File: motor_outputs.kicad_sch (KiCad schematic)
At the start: 9 parts, among them J2 Conn_01x08

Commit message: BOM work
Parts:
- F1: LCSC (none) -> C70114
- F2: renamed from F4; LCSC (none) -> C70114
- F3: renamed from F2; LCSC (none) -> C70114
- F4: renamed from F3; LCSC (none) -> C70114
- J3: renamed from J2; LCSC (none) -> C5137858
- renumbered D7 to D5, D5 to D6, D6 to D7
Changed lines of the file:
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@@
-	(wire
-		(pts
-			(xy 77.47 78.74) (xy 93.98 78.74)
-		)
-		(stroke
-			(width 0)
-			(type default)
-		)
-	)
-	(wire
-		(pts
-			(xy 77.47 73.66) (xy 77.47 78.74)
-		)
-		(stroke
-			(width 0)
-			(type default)
-		)
-	)
 	(wire
 		(pts
@@
 	(wire
 		(pts
-			(xy 74.93 73.66) (xy 77.47 73.66)
-		)
-		(stroke
-			(width 0)
-			(type default)
-		)
-	)
-	(wire
-		(pts
-			(xy 99.06 50.8) (xy 99.06 85.09)
+			(xy 74.93 73.66) (xy 92.71 73.66)
+		)
+		(stroke
+			(width 0)
+			(type default)
+		)
+	)
+	(wire
+		(pts
+			(xy 99.06 46.99) (xy 99.06 85.09)
 		)
 		(stroke
@@
 	(wire
 		(pts
-			(xy 93.98 90.17) (xy 99.06 90.17)
+			(xy 92.71 90.17) (xy 99.06 90.17)
 		)
 		(stroke
@@
 	(wire
 		(pts
-			(xy 93.98 78.74) (xy 93.98 90.17)
+			(xy 92.71 73.66) (xy 92.71 90.17)
 		)
 		(stroke
@@
 	(wire
 		(pts
-			(xy 74.93 46.99) (xy 71.12 46.99)
+			(xy 71.12 46.99) (xy 99.06 46.99)
 		)
 		(stroke
@@
 		(pts
 			(xy 99.06 130.81) (xy 99.06 102.87)
-		)
-		(stroke
-			(width 0)
-			(type default)
-		)
-	)
-	(wire
-		(pts
-			(xy 74.93 50.8) (xy 74.93 46.99)
-		)
-		(stroke
-			(width 0)
-			(type default)
-		)
-	)
-	(wire
-		(pts
-			(xy 74.93 50.8) (xy 99.06 50.8)
 		)
 		(stroke
@@
 		(exclude_from_sim no)
 		(in_bom yes)
-		(on_board yes)
+		(on_board no)
 		(dnp no)
 		(fields_autoplaced yes)
-		(property "Reference" "F3"
+		(property "Reference" "F4"
 			(at 69.85 92.71 90)
 			(effects
@@
 		(property "Description" "Resettable fuse, polymeric positive temperature coefficient"
 			(at 69.85 99.06 0)
+			(effects
+				(font
+					(size 1.27 1.27)
+				)
+				(hide yes)
+			)
+		)
+		(property "LCSC" "C70114"
+			(at 69.85 99.06 90)
 			(effects
 				(font
@@
 			(project "barn-blinds-controller"
 				(path "/aa90962a-81b9-423d-8acd-c4e83fa798bb/4857807b-67c7-42cb-aab6-84b757102806"
-					(reference "F3")
+					(reference "F4")
 					(unit 1)
 				)
@@
 		(exclude_from_sim no)
 		(in_bom yes)
-		(on_board yes)
+		(on_board no)
 		(dnp no)
 		(fields_autoplaced yes)
-		(property "Reference" "F4"
+		(property "Reference" "F2"
 			(at 67.31 116.84 90)
 			(effects
@@
 		(property "Description" "Resettable fuse, polymeric positive temperature coefficient"
 			(at 67.31 123.19 0)
+			(effects
+				(font
+					(size 1.27 1.27)
+				)
+				(hide yes)
+			)
+		)
+		(property "LCSC" "C70114"
+			(at 67.31 123.19 90)
 			(effects
 				(font
@@
 			(project "barn-blinds-controller"
 				(path "/aa90962a-81b9-423d-8acd-c4e83fa798bb/4857807b-67c7-42cb-aab6-84b757102806"
-					(reference "F4")
+					(reference "F2")
 					(unit 1)
 				)
@@
 		(dnp no)
 		(fields_autoplaced yes)
-		(property "Reference" "D7"
+		(property "Reference" "D5"
 			(at 76.2 125.7299 0)
 			(effects
@@
 			(project "barn-blinds-controller"
 				(path "/aa90962a-81b9-423d-8acd-c4e83fa798bb/4857807b-67c7-42cb-aab6-84b757102806"
-					(reference "D7")
+					(reference "D5")
 					(unit 1)
 				)
@@
 		(exclude_from_sim no)
 		(in_bom yes)
-		(on_board yes)
+		(on_board no)
 		(dnp no)
 		(fields_autoplaced yes)
-		(property "Reference" "F2"
+		(property "Reference" "F3"
 			(at 69.85 67.31 90)
 			(effects
@@
 		(property "Description" "Resettable fuse, polymeric positive temperature coefficient"
 			(at 69.85 73.66 0)
+			(effects
+				(font
+					(size 1.27 1.27)
+				)
+				(hide yes)
+			)
+		)
+		(property "LCSC" "C70114"
+			(at 69.85 73.66 90)
 			(effects
 				(font
@@
 			(project "barn-blinds-controller"
 				(path "/aa90962a-81b9-423d-8acd-c4e83fa798bb/4857807b-67c7-42cb-aab6-84b757102806"
-					(reference "F2")
+					(reference "F3")
 					(unit 1)
 				)
@@
 		(dnp no)
 		(fields_autoplaced yes)
-		(property "Reference" "D5"
+		(property "Reference" "D6"
 			(at 78.74 76.1999 0)
 			(effects
@@
 			(project "barn-blinds-controller"
 				(path "/aa90962a-81b9-423d-8acd-c4e83fa798bb/4857807b-67c7-42cb-aab6-84b757102806"
-					(reference "D5")
+					(reference "D6")
 					(unit 1)
 				)
@@
 		(on_board yes)
 		(dnp no)
-		(property "Reference" "J2"
+		(property "Reference" "J3"
 			(at 106.68 95.2501 0)
 			(effects
@@
 		)
 		(property "Description" "Generic connector, single row, 01x08, script generated (kicad-library-utils/schlib/autogen/connector/)"
+			(at 104.14 95.25 0)
+			(effects
+				(font
+					(size 1.27 1.27)
+				)
+				(hide yes)
+			)
+		)
+		(property "LCSC" "C5137858"
 			(at 104.14 95.25 0)
 			(effects
@@
 			(project "barn-blinds-controller"
 				(path "/aa90962a-81b9-423d-8acd-c4e83fa798bb/4857807b-67c7-42cb-aab6-84b757102806"
-					(reference "J2")
+					(reference "J3")
 					(unit 1)
 				)
@@
 		(dnp no)
 		(fields_autoplaced yes)
-		(property "Reference" "D6"
+		(property "Reference" "D7"
 			(at 80.01 101.5999 0)
 			(effects
@@
 			(project "barn-blinds-controller"
 				(path "/aa90962a-81b9-423d-8acd-c4e83fa798bb/4857807b-67c7-42cb-aab6-84b757102806"
-					(reference "D6")
+					(reference "D7")
 					(unit 1)
 				)
@@
 		(exclude_from_sim no)
 		(in_bom yes)
-		(on_board yes)
+		(on_board no)
 		(dnp no)
 		(fields_autoplaced yes)
@@
 			(effects
 				(font
+					(size 1.27 1.27)
+				)
+				(hide yes)
+			)
+		)
+		(property "LCSC" "C70114"
+			(at 66.04 54.61 90)
+			(effects
+				(font

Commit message: Updated BOM, fixed a few components
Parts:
- F1, F2, F3, F4: LCSC C70114 -> C69691
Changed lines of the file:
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@@
 		(exclude_from_sim no)
 		(in_bom yes)
-		(on_board no)
+		(on_board yes)
 		(dnp no)
 		(fields_autoplaced yes)
@@
 			)
 		)
-		(property "LCSC" "C70114"
+		(property "LCSC" "C69691"
 			(at 69.85 99.06 90)
 			(effects
@@
 		(exclude_from_sim no)
 		(in_bom yes)
-		(on_board no)
+		(on_board yes)
 		(dnp no)
 		(fields_autoplaced yes)
@@
 			)
 		)
-		(property "LCSC" "C70114"
+		(property "LCSC" "C69691"
 			(at 67.31 123.19 90)
 			(effects
@@
 		(exclude_from_sim no)
 		(in_bom yes)
-		(on_board no)
+		(on_board yes)
 		(dnp no)
 		(fields_autoplaced yes)
@@
 			)
 		)
-		(property "LCSC" "C70114"
+		(property "LCSC" "C69691"
 			(at 69.85 73.66 90)
 			(effects
@@
 		(exclude_from_sim no)
 		(in_bom yes)
-		(on_board no)
+		(on_board yes)
 		(dnp no)
 		(fields_autoplaced yes)
@@
 			)
 		)
-		(property "LCSC" "C70114"
+		(property "LCSC" "C69691"
 			(at 66.04 54.61 90)
 			(effects

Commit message: Sent for production
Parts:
- J3: footprint barn_shade_controller:TerminalBlock_JL271R-35008G01_Spring_1x08_P3.50mm_Horizontal -> barn_shade_controller:CONN-TH_8P-P3.50_JL271R-35008G01; symbol Connector_Generic:Conn_01x08 -> New_Library:JL271R-35008G01; LCSC Part Name (none) -> 1x8P 3.5mm 每排P数:8 排数:1; Manufacturer (none) -> JILN(锦凌); Manufacturer Part (none) -> JL271R-35008G01; Supplier (none) -> LCSC; Supplier Part (none) -> C5137858
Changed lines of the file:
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@@
+	(wire
+		(pts
+			(xy 99.06 102.87) (xy 99.06 130.81)
+		)
+		(stroke
+			(width 0)
+			(type default)
+		)
+	)
 	(wire
 		(pts
@@
 		(pts
 			(xy 71.12 46.99) (xy 99.06 46.99)
-		)
-		(stroke
-			(width 0)
-			(type default)
-		)
-	)
-	(wire
-		(pts
-			(xy 99.06 130.81) (xy 99.06 102.87)
 		)
 		(stroke
@@
 	)
 	(symbol
-		(lib_id "Connector_Generic:Conn_01x08")
-		(at 104.14 95.25 0)
+		(lib_id "New_Library:JL271R-35008G01")
+		(at 104.14 93.98 0)
 		(mirror x)
 		(unit 1)
@@
 		(dnp no)
 		(property "Reference" "J3"
-			(at 106.68 95.2501 0)
+			(at 106.68 93.9801 0)
 			(effects
 				(font
@@
 		)
 		(property "Value" "Conn_01x08"
-			(at 106.68 92.7101 0)
+			(at 106.68 91.4401 0)
 			(effects
 				(font
@@
 			)
 		)
-		(property "Footprint" "barn_shade_controller:TerminalBlock_JL271R-35008G01_Spring_1x08_P3.50mm_Horizontal"
-			(at 104.14 95.25 0)
-			(effects
-				(font
-					(size 1.27 1.27)
-				)
-				(hide yes)
-			)
-		)
-		(property "Datasheet" "~"
-			(at 104.14 95.25 0)
-			(effects
-				(font
-					(size 1.27 1.27)
-				)
-				(hide yes)
-			)
-		)
-		(property "Description" "Generic connector, single row, 01x08, script generated (kicad-library-utils/schlib/autogen/connector/)"
-			(at 104.14 95.25 0)
+		(property "Footprint" "barn_shade_controller:CONN-TH_8P-P3.50_JL271R-35008G01"
+			(at 104.14 93.98 0)
+			(effects
+				(font
+					(size 1.27 1.27)
+				)
+				(hide yes)
+			)
+		)
+		(property "Datasheet" "https://item.szlcsc.com/datasheet/JL271R-35008G01/5747791.html"
+			(at 104.14 93.98 0)
+			(effects
+				(font
+					(size 1.27 1.27)
+				)
+				(hide yes)
+			)
+		)
+		(property "Description" "Number of Positions or Pins:1x8P Pitch:3.5mm Color:Green Mounting Type:Right Angle Number of Pins:8P Number of PINs Per Row:8 Number of Rows:1 Current Rating:10A Voltage Rating (Max):300V Wire Gauge - AWG:16~24 Wire Gauge - mm2:0.2~1.5 Operating Temperatu"
+			(at 104.14 93.98 0)
 			(effects
 				(font
@@
 		)
 		(property "LCSC" "C5137858"
-			(at 104.14 95.25 0)
-			(effects
-				(font
+			(at 104.14 93.98 0)
+			(effects
+				(font
+					(size 1.27 1.27)
+				)
+				(hide yes)
+			)
+		)
+		(property "Manufacturer Part" "JL271R-35008G01"
+			(at 104.14 93.98 0)
+			(effects
+				(font
+					(size 1.27 1.27)
+				)
+				(hide yes)
+			)
+		)
+		(property "Manufacturer" "JILN(锦凌)"
+			(at 104.14 93.98 0)
+			(effects
+				(font
+					(size 1.27 1.27)
+				)
+				(hide yes)
+			)
+		)
+		(property "Supplier Part" "C5137858"
+			(at 104.14 93.98 0)
+			(effects
+				(font
+					(size 1.27 1.27)
+				)
+				(hide yes)
+			)
+		)
+		(property "Supplier" "LCSC"
+			(at 104.14 93.98 0)
+			(effects
+				(font
+					(size 1.27 1.27)
+				)
+				(hide yes)
+			)
+		)
+		(property "LCSC Part Name" "1x8P 3.5mm 每排P数:8 排数:1"
+			(at 104.14 93.98 0)
+			(effects
+				(font

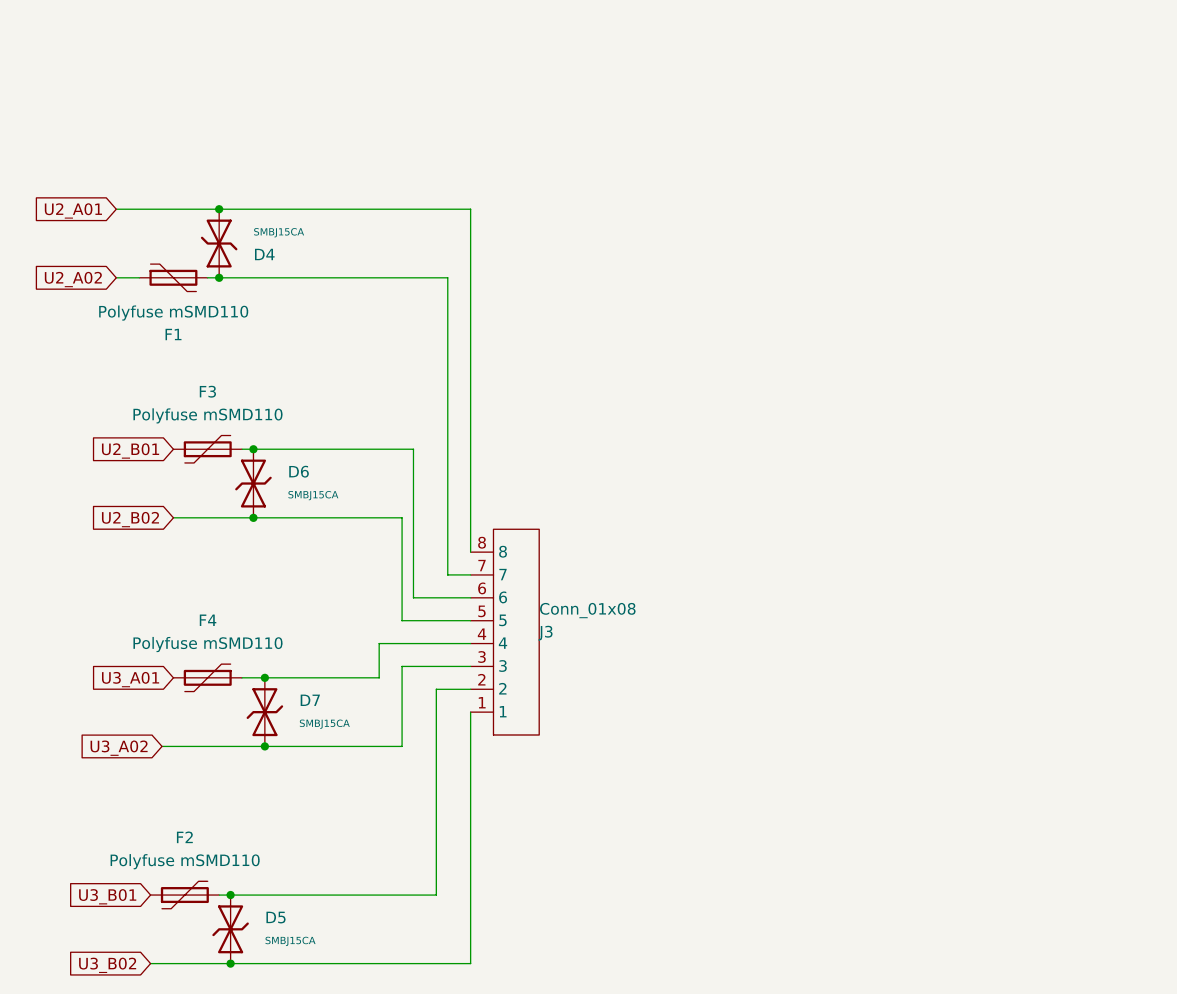
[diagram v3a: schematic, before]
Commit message: Refactored board to use larger vias and route better paths.
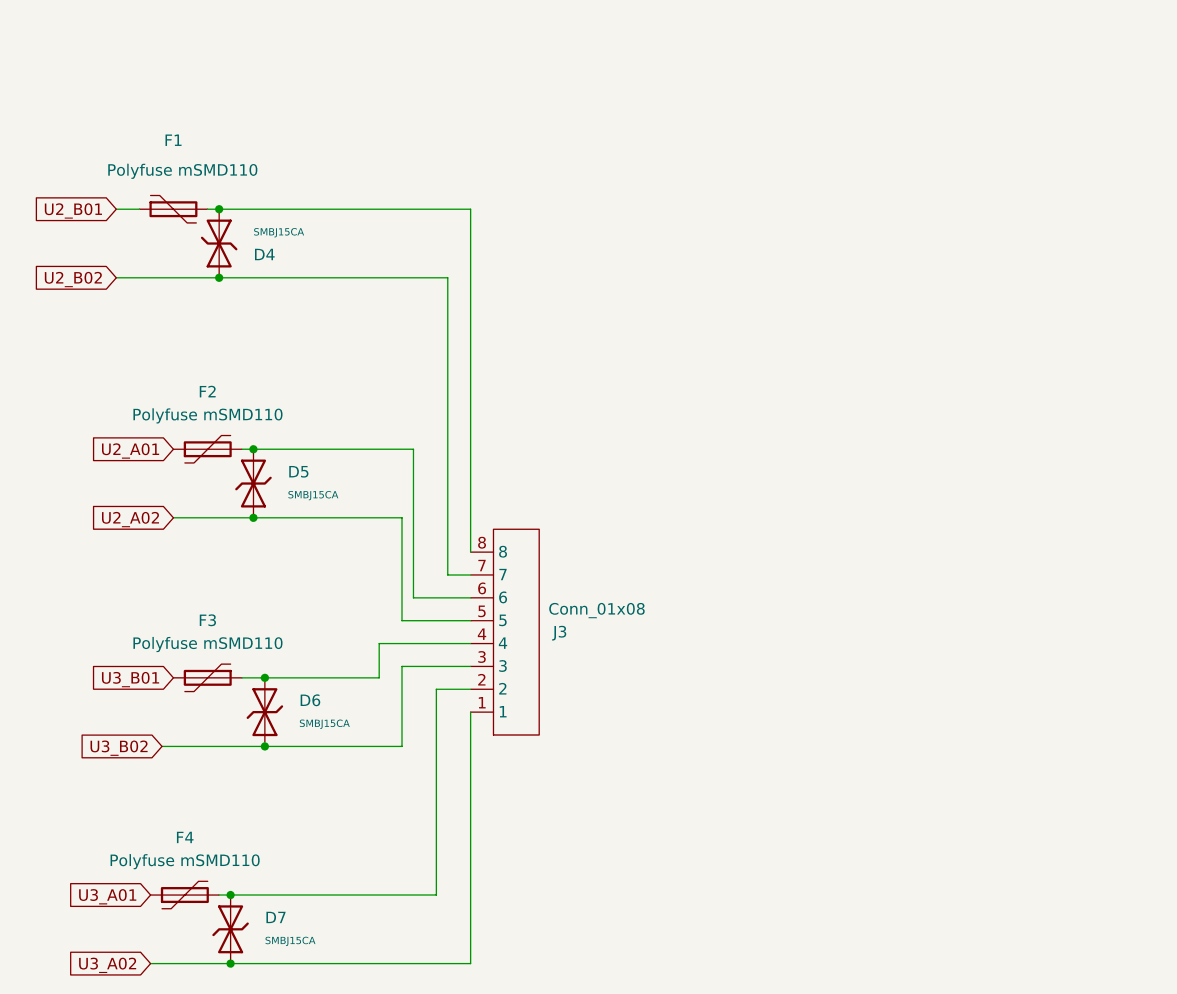
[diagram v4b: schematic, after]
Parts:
- renumbered D6 to D5, D7 to D6, D5 to D7, F3 to F2, F4 to F3, F2 to F4
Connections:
- net U2_A01: now also F2.1; no longer D4.1, J3.8
- net U2_A02: now also D5.1, J3.5; no longer F1.1
- net U2_B01: now also F1.1; no longer F2.1
- net U2_B02: now also D4.2, J3.7; no longer D5.1, J3.5
- net U3_A01: now also F4.1; no longer F3.2
- net U3_A02: now also D7.1, J3.1; no longer D6.1, J3.3
- net U3_B01: now also F3.2; no longer F4.1
- net U3_B02: now also D6.1, J3.3; no longer D7.1, J3.1
- new net: D4.1, F1.2, J3.8
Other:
- moved on the sheet: F1

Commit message: V 1.2
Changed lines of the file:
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@@
 	(paper "A4")
+	(junction
+		(at 76.2 106.68)
+		(diameter 0)
+		(color 0 0 0 0)
+	)
+	(junction
+		(at 74.93 73.66)
+		(diameter 0)
+		(color 0 0 0 0)
+	)
+	(junction
+		(at 72.39 130.81)
+		(diameter 0)
+		(color 0 0 0 0)
+	)
+	(junction
+		(at 72.39 123.19)
+		(diameter 0)
+		(color 0 0 0 0)
+	)
+	(junction
+		(at 74.93 81.28)
+		(diameter 0)
+		(color 0 0 0 0)
+	)
+	(junction
+		(at 71.12 46.99)
+		(diameter 0)
+		(color 0 0 0 0)
+	)
 	(junction
 		(at 71.12 54.61)
@@
 	)
 	(junction
-		(at 71.12 46.99)
-		(diameter 0)
-		(color 0 0 0 0)
-	)
-	(junction
-		(at 76.2 106.68)
-		(diameter 0)
-		(color 0 0 0 0)
-	)
-	(junction
-		(at 74.93 73.66)
-		(diameter 0)
-		(color 0 0 0 0)
-	)
-	(junction
-		(at 72.39 130.81)
-		(diameter 0)
-		(color 0 0 0 0)
-	)
-	(junction
-		(at 72.39 123.19)
-		(diameter 0)
-		(color 0 0 0 0)
-	)
-	(junction
-		(at 74.93 81.28)
-		(diameter 0)
-		(color 0 0 0 0)
-	)
-	(junction
 		(at 76.2 99.06)
 		(diameter 0)
@@
 	(wire
 		(pts
+			(xy 71.12 46.99) (xy 99.06 46.99)
+		)
+		(stroke
+			(width 0)
+			(type default)
+		)
+	)
+	(wire
+		(pts
 			(xy 71.12 123.19) (xy 72.39 123.19)
 		)
@@
 	(wire
 		(pts
+			(xy 71.12 54.61) (xy 96.52 54.61)
+		)
+		(stroke
+			(width 0)
+			(type default)
+		)
+	)
+	(wire
+		(pts
 			(xy 73.66 99.06) (xy 76.2 99.06)
 		)
@@
 	(wire
 		(pts
-			(xy 71.12 54.61) (xy 96.52 54.61)
-		)
-		(stroke
-			(width 0)
-			(type default)
-		)
-	)
-	(wire
-		(pts
 			(xy 92.71 90.17) (xy 99.06 90.17)
 		)
@@
 		(pts
 			(xy 88.9 99.06) (xy 88.9 95.25)
-		)
-		(stroke
-			(width 0)
-			(type default)
-		)
-	)
-	(wire
-		(pts
-			(xy 71.12 46.99) (xy 99.06 46.99)
 		)
 		(stroke
@@
 		(fields_autoplaced yes)
 		(property "Reference" "D4"
-			(at 74.93 52.0701 0)
-			(effects
-				(font
-					(size 1.27 1.27)
-				)
-				(justify left)
+			(at 67.31 49.5299 0)
+			(effects
+				(font
+					(size 1.27 1.27)
+				)
+				(justify right)
 			)
 		)
 		(property "Value" "SMBJ15CA"
-			(at 74.93 49.53 0)
+			(at 67.31 52.07 0)
 			(effects
 				(font
 					(size 0.8 0.8)
 				)
-				(justify left)
-			)
-		)
+				(justify right)
+			)
+		)

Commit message: Rev 1.3 updates
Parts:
- removed J3: Conn_01x08, barn_shade_controller:CONN-TH_8P-P3.50_JL271R-35008G01, symbol New_Library:JL271R-35008G01
- added J3: 1054070, 1054070:1054070, symbol 1054070:1054070
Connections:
- net U2_A02: now also J3.11
- net M4_OUTA: now reaches D6.2, F3.1
- net M3_OUTA: now reaches D7.2, F4.2
- net M1_OUTA: now reaches D5.2, F2.2
- net M1_OUTA: now also J3.1
- net M2_OUTA: now reaches D4.1, F1.2
